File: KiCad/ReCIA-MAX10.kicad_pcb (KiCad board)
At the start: 4 copper layers, 17.4 x 51.4 mm, 29 parts, among them J1 Conn_02x03_Odd_Even, U1 AMS1117-3.3, U2 SN74CBT16210, U3 SN74CBT16210, U4 10M02SCU169, U5 8520_DIP_SOCKET, X1 Oscillator_3.2x2.5mm-28.6363M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

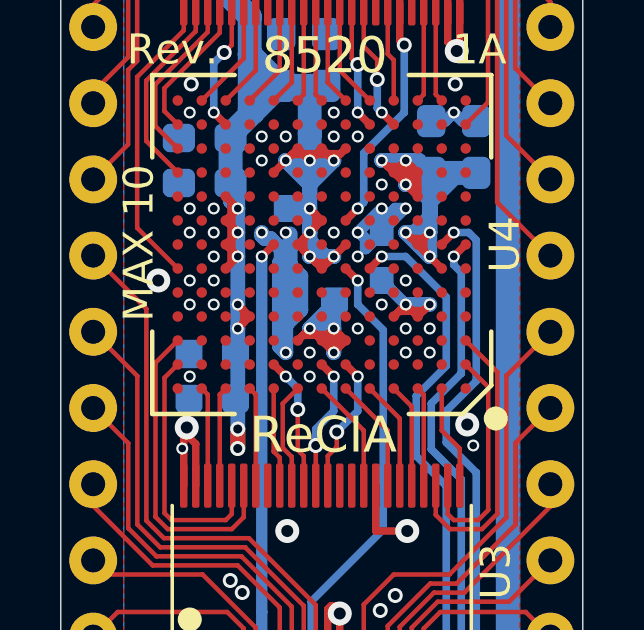
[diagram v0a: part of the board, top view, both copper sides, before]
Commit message: Assign GND to CONFIG_SEL pad
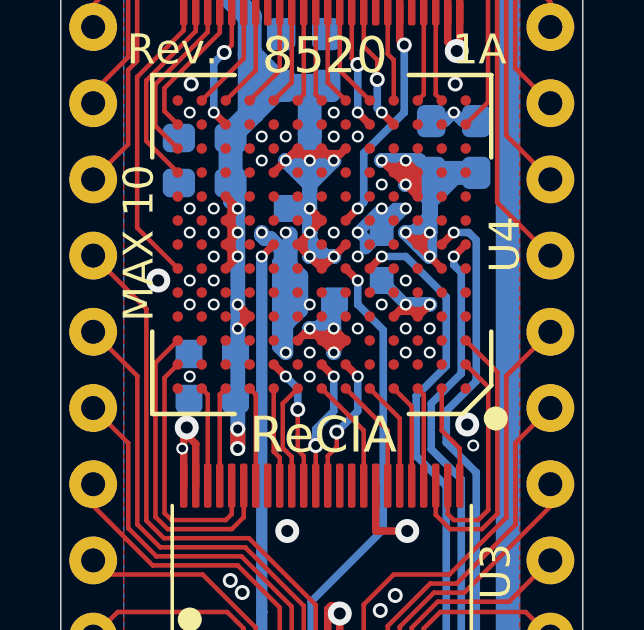
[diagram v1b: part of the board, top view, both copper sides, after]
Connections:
- U4 pad D7: Net-(U4-PadD7) -> GND
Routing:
- net GND: vias 83 -> 84

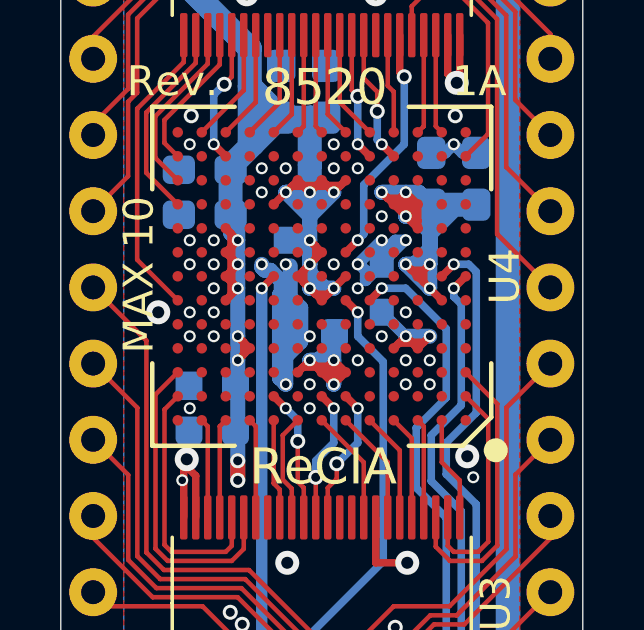
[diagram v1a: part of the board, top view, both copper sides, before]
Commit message: Add nCONFIG signal
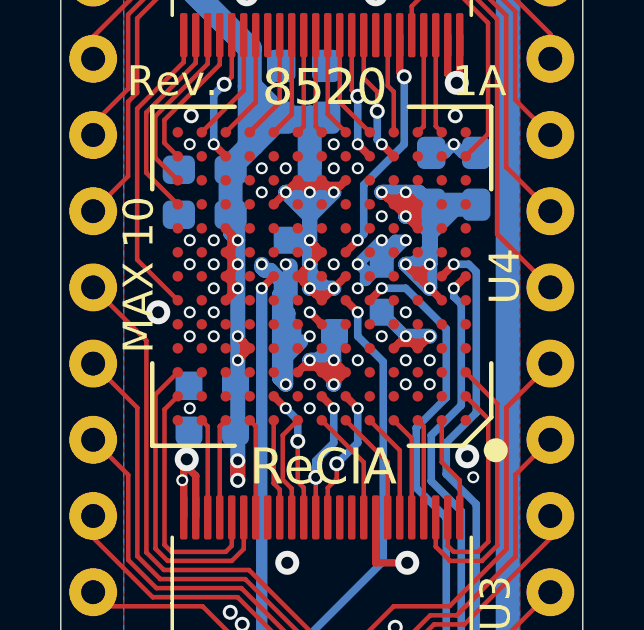
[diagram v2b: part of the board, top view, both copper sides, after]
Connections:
- net Net-(U4-PadE7) renamed nCONFIG
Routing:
- net nCONFIG: track 0.00 -> 15.5 mm, vias 0 -> 1
- net GND: track 46.6 -> 44.6 mm

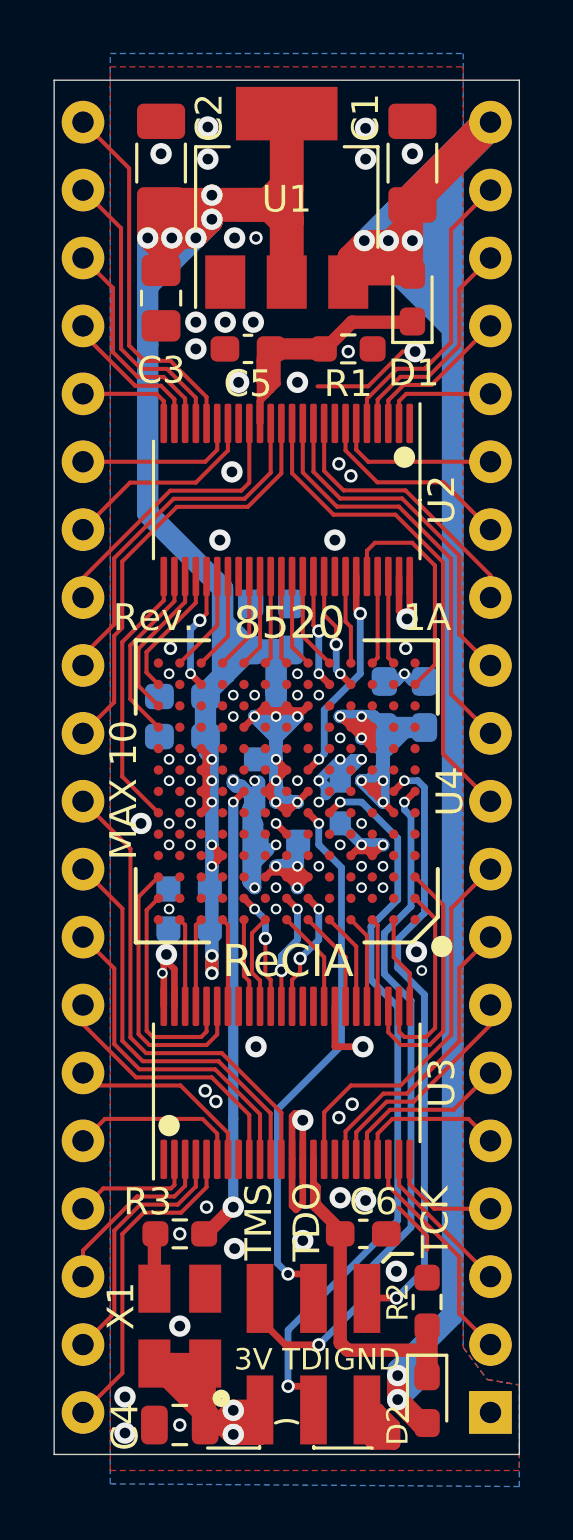
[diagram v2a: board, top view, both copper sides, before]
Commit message: Add nSTATUS signal
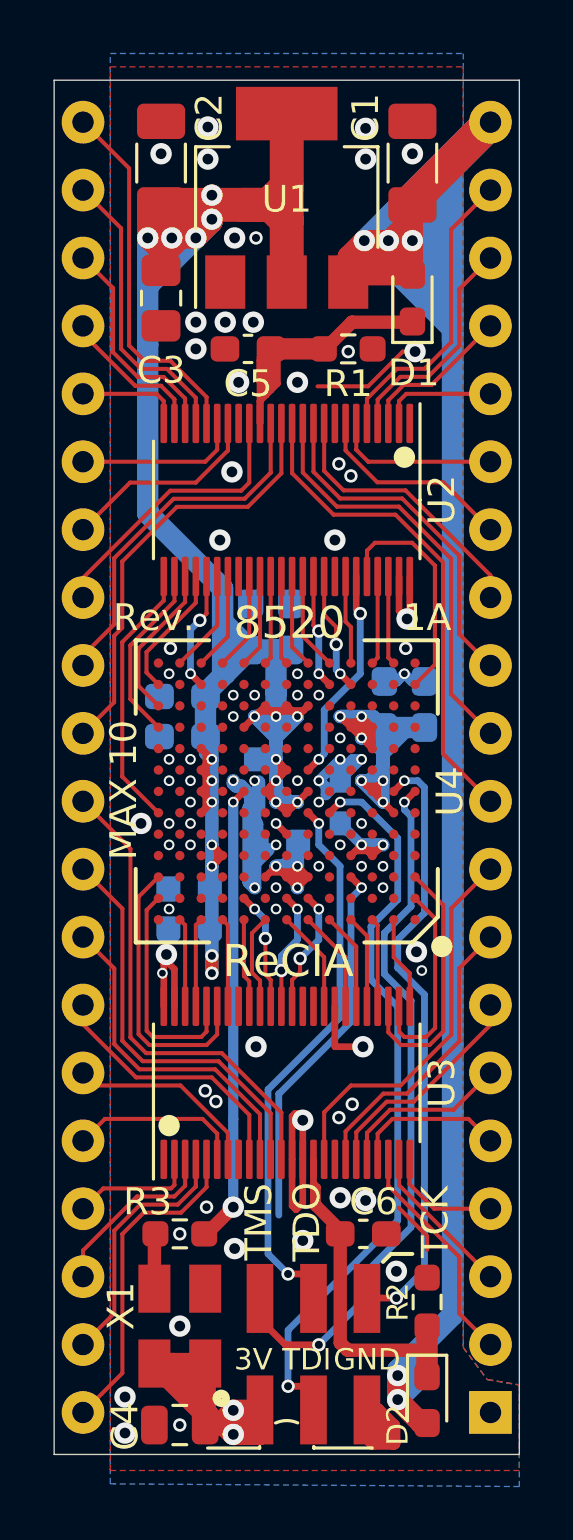
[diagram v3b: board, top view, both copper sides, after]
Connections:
- net Net-(U4-PadC4) renamed nSTATUS
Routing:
- net nSTATUS: track 0.00 -> 14.1 mm, vias 0 -> 1
- net GND: vias 84 -> 83

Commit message: Add CONF_DONE signal
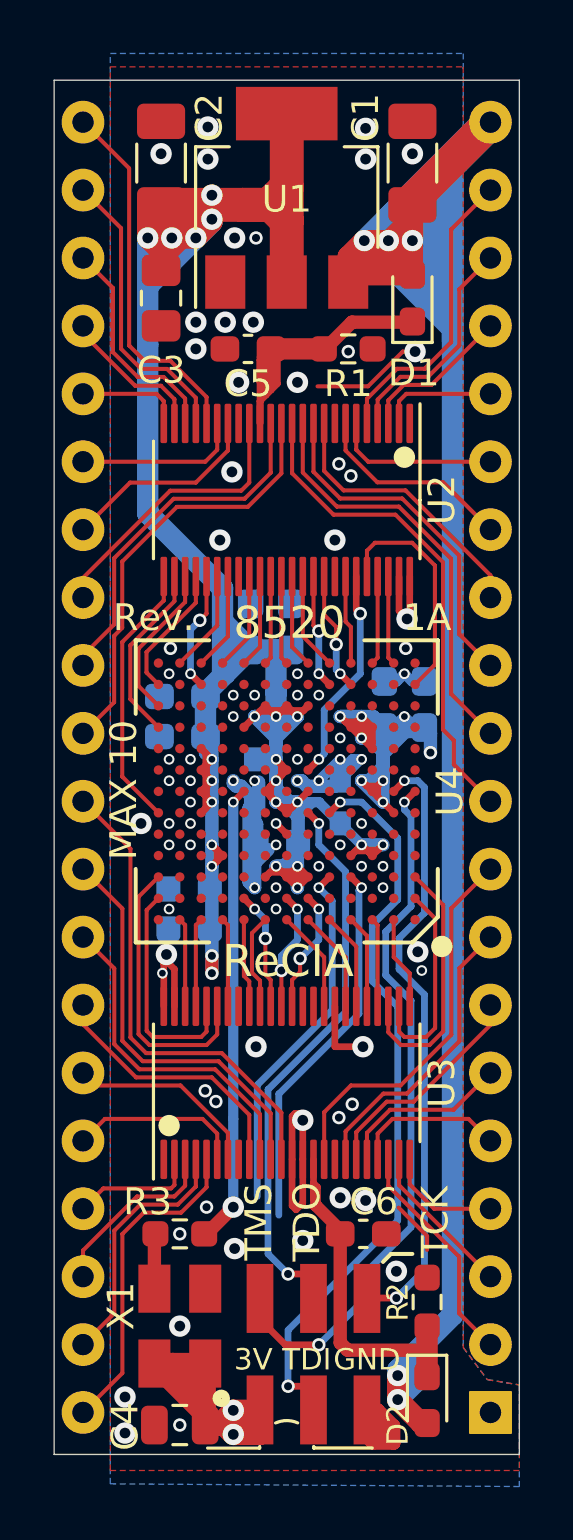
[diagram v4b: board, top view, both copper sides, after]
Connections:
- net Net-(U4-PadC5) renamed CONF_DONE
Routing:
- net CONF_DONE: track 0.00 -> 13.5 mm, vias 0 -> 1
- net 3V3: track 184.3 -> 192.1 mm, vias 32 -> 34

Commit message: Add 10k resistor pack RN1 and assign pull-ups for TMS, TDI and pull-down for TCK
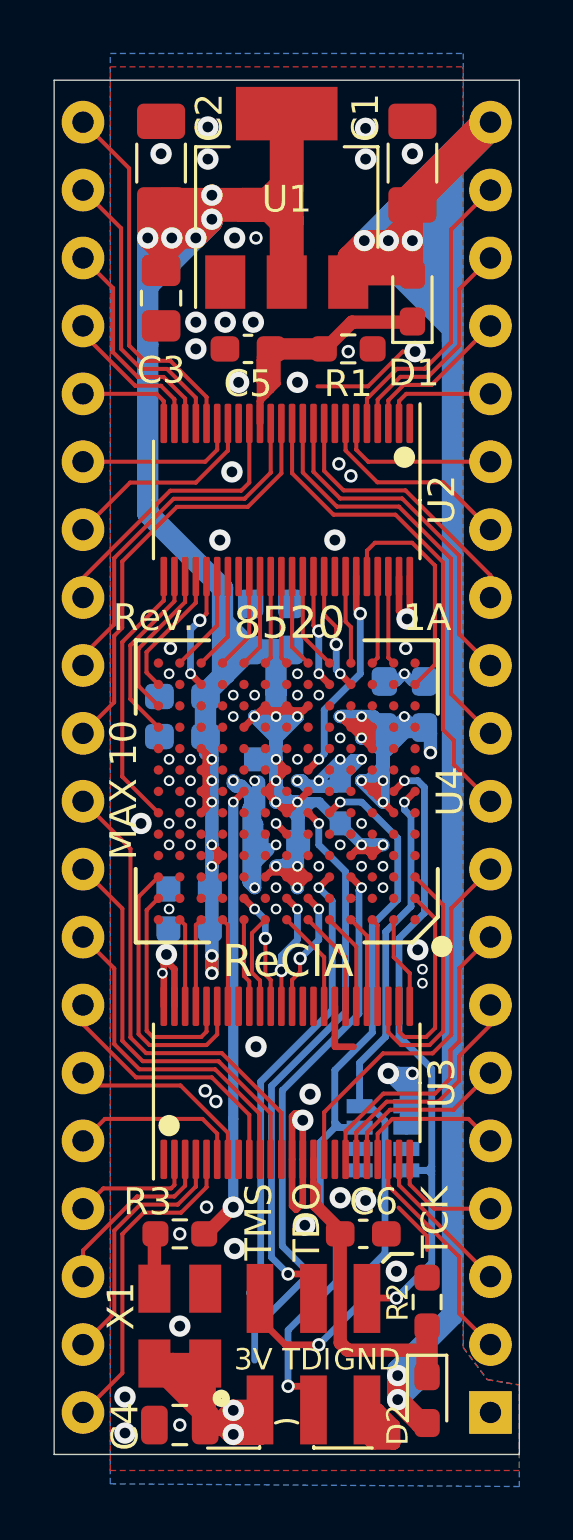
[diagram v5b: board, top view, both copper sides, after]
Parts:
- added RN1: R_Pack04, ReCIA:RESCAF80P320X160X60-8N, B.Cu at (135.6, 96.9)
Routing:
- net 3V3: track 192.1 -> 198.6 mm, vias 34 -> 36
- net nSTATUS: track 14.1 -> 20.6 mm
- net CONF_DONE: track 13.5 -> 17.2 mm
- net TCK: track 22.8 -> 25.3 mm
- net TDI: track 28.0 -> 29.7 mm
- net PA6: track 11.1 -> 11.7 mm
- net PA5: track 8.44 -> 8.98 mm
- net GND: vias 83 -> 82
